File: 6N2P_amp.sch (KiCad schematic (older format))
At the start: 39 parts, among them J1 6.3MMTRSSwitched, U1 ECC83, U2 ECC83

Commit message: snap
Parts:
- added C14: 470p, Capacitor_THT:C_Rect_L9.0mm_W4.0mm_P7.50mm_MKT, symbol Device:C
- added C15: 22n, Capacitor_THT:C_Rect_L9.0mm_W4.0mm_P7.50mm_MKT, symbol Device:C
- added C16: 10n, Capacitor_THT:C_Rect_L9.0mm_W4.0mm_P7.50mm_MKT, symbol Device:C
- added R18, R19, R21, R22, R? (x2): LDR03, OptoDevice:R_LDR_10x8.5mm_P7.6mm_Vertical, symbol Sensor_Optical:LDR03
- added R20: 56k, Resistor_THT:R_Axial_DIN0207_L6.3mm_D2.5mm_P10.16mm_Horizontal, symbol Device:R
- added RV10: 50k lin, symbol Device:R_POT
- added RV11: 1M log, symbol Device:R_POT
- added RV7, RV9: 500k log, symbol Device:R_POT
- added RV8: 250k lin, symbol Device:R_POT
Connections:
- net GND: now also RV10.3, RV11.3, RV7.3
- net at C5.2, R7.2, U1.1 (A): now also R?.2
- net at C2.1, RV1.1: now also RV7.1
- net at C3.2, R4.2: now also R18.1, R19.1; no longer RV1.2
- net at R15.2, U2.6 (A): now also R?.2; no longer U2.2 (G)
- net at C11.2, R16.1, R17.1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: now also C14.2, R20.1
- net at RV6.2: now also R21.2
- new net: R18.2, RV1.2
- new net: R?.1, R?.1, U2.2 (G)
- new net: R19.2, RV7.2
- new net: RV10.1, RV9.3
- new net: C16.1, RV10.2
- new net: C15.1, RV8.3, RV9.1, RV9.2
- new net: C15.2, C16.2, R20.2
- new net: C14.1, RV8.1
- new net: RV11.1, RV8.2
- new net: R22.2, RV11.2
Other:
- note added: "clean channel"
- note added: "overdrive channel"
- moved on the sheet: C10, C11, C12, C13, C2, C3, C5, R14, R15, R17, R4, R5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

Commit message: it is making progress
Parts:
- added J2: 6.3MMTRSSwitched, micha_custom:Reichelt_EBS63P, symbol micha_custom:6.3MMTRSSwitched
- added R25, R29: 0R, Resistor_THT:R_Axial_DIN0207_L6.3mm_D2.5mm_P10.16mm_Horizontal, symbol Device:R
- added R26, R30: DNP, Resistor_THT:R_Axial_DIN0207_L6.3mm_D2.5mm_P10.16mm_Horizontal, symbol Device:R
- added R27: 5.6k, Resistor_THT:R_Axial_DIN0207_L6.3mm_D2.5mm_P10.16mm_Horizontal, symbol Device:R
- added R28, R31: 470R/1W, Resistor_THT:R_Axial_DIN0207_L6.3mm_D2.5mm_P10.16mm_Horizontal, symbol Device:R
- added TR1: TRANSF1, symbol Transformer:TRANSF1
- added U3: 6N1P, Valve:Valve_Noval_P, symbol micha_custom:6N1P
- gave numbers to parts that had none: 2
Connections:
- net GND: now also U1.9 (F2), U2.9 (F2), R26.1, R28.1, R30.1, U3.4 (F1), U3.9 (F2)
- net HV_C: now reaches C6.1, R10.2, R3.1, R7.1
- net at U1.4 (F1): now also R25.2, R26.2
- net 6.3V: now reaches U1.5 (F1)
- net 6.3V: now also U2.5 (F1), R25.1, R29.1, U3.5 (F1)
- net HV_B: now reaches C7.1, R10.1, R11.2, R15.1, U2.1 (A)
- net at U2.4 (F1): now also R29.2, R30.2
- net HV_A: now reaches C8.1, R11.1, R12.2
- net HV_A: now also TR1.2
- net HV_in: now reaches C9.1, R12.1, R13.2
- net at R22.1: now also R21.1, R27.2
- new net: TR1.1, U3.1 (A), U3.6 (A)
- new net: R27.1, U3.2 (G), U3.7 (G)
- new net: R28.2, U3.3 (K), U3.8 (K)
- new net: J2.3 (Sleeve), R31.2, TR1.3
- new net: J2.1 (Tip), TR1.4
- new net: J2.4 (TipSwitch), R31.1
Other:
- note added: "1W Power Amplifier"
- note added: "if U1 is 6N2P then\nR26=0R, R25=DNP"
- note removed: "6.3 between 4,5 for 6N2P"
- moved on the sheet: U2C

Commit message: some progress ... made symbols for dc dc converters and transformer
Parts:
- removed TR1: TRANSF1, symbol Transformer:TRANSF1
- added J? (x2): 6.3MMTRSSwitched, micha_custom:Reichelt_EBS63P, symbol micha_custom:6.3MMTRSSwitched
- added U? (x3): DSN-MINI-360, micha_custom:DSN-MINI-360, symbol micha_custom:DSN-MINI-360
- added U?: NCH6100HV, micha_custom:NCH6100HV, symbol micha_custom:NCH6100HV
- R31: value 470R/1W -> 8R/1W
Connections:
- net GND: now also J?.3 (Sleeve), J?.3 (Sleeve), U?.1 (GND), U?.2 (OUT-), U?.2 (OUT-), U?.2 (OUT-), U?.3 (IN-), U?.3 (IN-), U?.3 (IN-), U?.4 (GND)
- net HV_in: now also U?.5 (HV)
- net at R21.1, R22.1: now also J?.1 (Tip), J?.4 (TipSwitch); no longer R27.2
- removed net 6.3V: R25.1, R29.1, U1.5 (F1), U2.5 (F1), U3.5 (F1)
- new net: J?.1 (Tip), R27.2
- new net 12V: U?.3 (VIN), U?.4 (IN+), U?.4 (IN+), U?.4 (IN+)
- new net 6.3V_U1: R25.1, U1.5 (F1), U?.1 (OUT+)
- new net 6.3V_U2: R29.1, U2.5 (F1), U?.1 (OUT+)
- new net 6.3V_U3: U3.5 (F1), U?.1 (OUT+)
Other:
- note added: "FX return"
- note added: "FX send"
- note added: "adjust output\nto 6.3V !!!"
- moved on the sheet: C1, C10, C11, C12, C13, C14, C15, C16, C2, C3, C4, C5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

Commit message: snap, ... started experimental routing
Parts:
- removed U? (x3): DSN-MINI-360, micha_custom:DSN-MINI-360, symbol micha_custom:DSN-MINI-360
- added R32: DNP, Resistor_THT:R_Axial_DIN0204_L3.6mm_D1.6mm_P2.54mm_Vertical, symbol Device:R
- added R33: 0R, Resistor_THT:R_Axial_DIN0204_L3.6mm_D1.6mm_P2.54mm_Vertical, symbol Device:R
- added TR1: VISATON_TR_10.16, micha_custom:VISATON_TR_10.16, symbol micha_custom:VISATON_TR_10.16
- added U4, U5, U6: DSN-MINI-360, micha_custom:DSN-MINI-360, symbol micha_custom:DSN-MINI-360
- J2: value 6.3MMTRSSwitched -> speaker
- J3: renamed from J?; value 6.3MMTRSSwitched -> fx_send
- J4: renamed from J?; value 6.3MMTRSSwitched -> fx_return
- R25, R26, R29, R30: footprint Resistor_THT:R_Axial_DIN0207_L6.3mm_D2.5mm_P10.16mm_Horizontal -> Resistor_THT:R_Axial_DIN0204_L3.6mm_D1.6mm_P2.54mm_Vertical
- RV1, RV10, RV11, RV2, RV3, RV4, RV5, RV6, RV7, RV8, RV9: footprint (none) -> Potentiometer_THT:Potentiometer_Alps_RK163_Single_Horizontal
- U3: footprint Valve:Valve_Noval_P -> w_vacuum:socket_gzc9-b
- gave numbers to parts that had none: 1
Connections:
- net 12V: now also U4.4 (IN+), U5.4 (IN+), U6.4 (IN+)
- net 6.3V_U1: now also U4.1 (OUT+)
- net 6.3V_U2: now also U5.1 (OUT+)
- net 6.3V_U3: now also R32.1, U6.1 (OUT+)
- net GND: now also RV1.1, RV10.1, RV11.1, RV2.1, RV5.1, RV6.1, RV7.1, R33.1, U4.2 (OUT-), U4.3 (IN-), U5.2 (OUT-), U5.3 (IN-), U6.2 (OUT-), U6.3 (IN-); no longer RV1.3, RV10.3, RV11.3, RV2.3, RV5.3, RV6.3, RV7.3, U3.4 (F1)
- net HV_A: now also TR1.2
- net at C5.1: now also RV2.3; no longer RV2.1
- net at RV4.3: now also C12.1, RV3.1, RV4.2; no longer RV5.1
- net at C11.1: now also RV3.3; no longer RV3.1
- net at RV3.2: now also RV6.3; no longer RV6.1
- net at RV9.3: now also C15.1, RV8.1, RV9.2; no longer RV10.1
- net at C14.1: now also RV8.3; no longer RV8.1
- net at RV8.2: now also RV11.3; no longer RV11.1
- net at U3.1 (A), U3.6 (A): now also TR1.1
- net at J2.1 (Tip): now also TR1.4
- net at J2.3 (Sleeve), R31.2: now also TR1.3
- new net: C2.1, RV1.3, RV7.3
- new net: RV4.1, RV5.3
- new net: RV10.3, RV9.1
- new net: R32.2, R33.2, U3.4 (F1)
- no-connect marks 3 -> 14
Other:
- moved on the sheet: U3C

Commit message: snap
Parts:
- J1: value 6.3MMTRSSwitched -> guitar_in
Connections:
- net guit_in: now reaches J1.1 (Tip), R1.1, U1.7 (G)
- net clean_channel_bypass: now reaches C5.2, R24.2, R7.2, U1.1 (A)
- net post_stage_1: now reaches C2.1, RV1.3, RV7.3
- net od_A: now reaches R15.2, R23.2, U2.6 (A)
- net fx_send: now reaches J3.1 (Tip), J4.4 (TipSwitch), R21.1, R22.1
- net power_anode: now reaches TR1.1, U3.1 (A), U3.6 (A)
- net spkr_n: now reaches J2.3 (Sleeve), R31.2, TR1.3
- net spkr_p: now reaches J2.1 (Tip), TR1.4
- net power_gate: now reaches R27.1, U3.2 (G), U3.7 (G)
- net power_cath: now reaches R28.2, U3.3 (K), U3.8 (K)
- net fx_return: now reaches J4.1 (Tip), R27.2
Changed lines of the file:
@@
 P 4100 8550
 F 0 "J1" H 4063 8697 60  0000 C CNN
-F 1 "6.3MMTRSSwitched" H 4063 8591 60  0000 C CNN
+F 1 "guitar_in" H 4063 8591 60  0000 C CNN
 F 2 "micha_custom:Reichelt_EBS63P" H 4100 8550 60  0001 C CNN
 F 3 "" H 4100 8550 60  0000 C CNN
@@
 NoConn ~ 2000 5600
 NoConn ~ 11250 3950
+Text Label 13600 3000 0    50   ~ 0
+fx_send
+Text Label 14050 3400 0    50   ~ 0
+fx_return
+Text Label 15100 4550 0    50   ~ 0
+power_anode
+Text Label 14900 5550 0    50   ~ 0
+power_gate
+Text Label 15000 5650 0    50   ~ 0
+power_cath
+Text Label 17300 4550 0    50   ~ 0
+spkr_p
+Text Label 17300 4750 0    50   ~ 0
+spkr_n
+Text Label 4900 8650 0    50   ~ 0
+guit_in
+Text Label 7150 8150 0    50   ~ 0
+post_stage_1
+Text Label 10850 12000 0    50   ~ 0
+clean_channel_bypass
+Text Label 12700 8150 0    50   ~ 0
+od_A
 $EndSCHEMATC

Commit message: snap
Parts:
- R25, R29: value 0R -> ECC83
- R26, R30: value DNP -> 6N2P
- R32: value DNP -> ECCXX
- R33: value 0R -> 6N1P
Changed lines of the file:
@@
 P 2000 2500
 F 0 "R25" V 1793 2500 50  0000 C CNN
-F 1 "0R" V 1884 2500 50  0000 C CNN
+F 1 "ECC83" V 1884 2500 50  0000 C CNN
 F 2 "Resistor_THT:R_Axial_DIN0204_L3.6mm_D1.6mm_P2.54mm_Vertical" V 1930 2500 50  0001 C CNN
 F 3 "~" H 2000 2500 50  0001 C CNN
@@
 P 2000 2650
 F 0 "R26" V 2150 2650 50  0000 C CNN
-F 1 "DNP" V 2250 2650 50  0000 C CNN
+F 1 "6N2P" V 2250 2650 50  0000 C CNN
 F 2 "Resistor_THT:R_Axial_DIN0204_L3.6mm_D1.6mm_P2.54mm_Vertical" V 1930 2650 50  0001 C CNN
 F 3 "~" H 2000 2650 50  0001 C CNN
@@
 P 2000 4000
 F 0 "R29" V 1793 4000 50  0000 C CNN
-F 1 "0R" V 1884 4000 50  0000 C CNN
+F 1 "ECC83" V 1884 4000 50  0000 C CNN
 F 2 "Resistor_THT:R_Axial_DIN0204_L3.6mm_D1.6mm_P2.54mm_Vertical" V 1930 4000 50  0001 C CNN
 F 3 "~" H 2000 4000 50  0001 C CNN
@@
 P 2000 4150
 F 0 "R30" V 2150 4150 50  0000 C CNN
-F 1 "DNP" V 2250 4150 50  0000 C CNN
+F 1 "6N2P" V 2250 4150 50  0000 C CNN
 F 2 "Resistor_THT:R_Axial_DIN0204_L3.6mm_D1.6mm_P2.54mm_Vertical" V 1930 4150 50  0001 C CNN
 F 3 "~" H 2000 4150 50  0001 C CNN
@@
 P 2000 5750
 F 0 "R33" V 2200 5750 50  0000 C CNN
-F 1 "0R" V 2100 5750 50  0000 C CNN
+F 1 "6N1P" V 2100 5750 50  0000 C CNN
 F 2 "Resistor_THT:R_Axial_DIN0204_L3.6mm_D1.6mm_P2.54mm_Vertical" V 1930 5750 50  0001 C CNN
 F 3 "~" H 2000 5750 50  0001 C CNN
@@
 P 2000 5600
 F 0 "R32" V 1900 5600 50  0000 C CNN
-F 1 "DNP" V 1800 5600 50  0000 C CNN
+F 1 "ECCXX" V 1800 5600 50  0000 C CNN
 F 2 "Resistor_THT:R_Axial_DIN0204_L3.6mm_D1.6mm_P2.54mm_Vertical" V 1930 5600 50  0001 C CNN
 F 3 "~" H 2000 5600 50  0001 C CNN

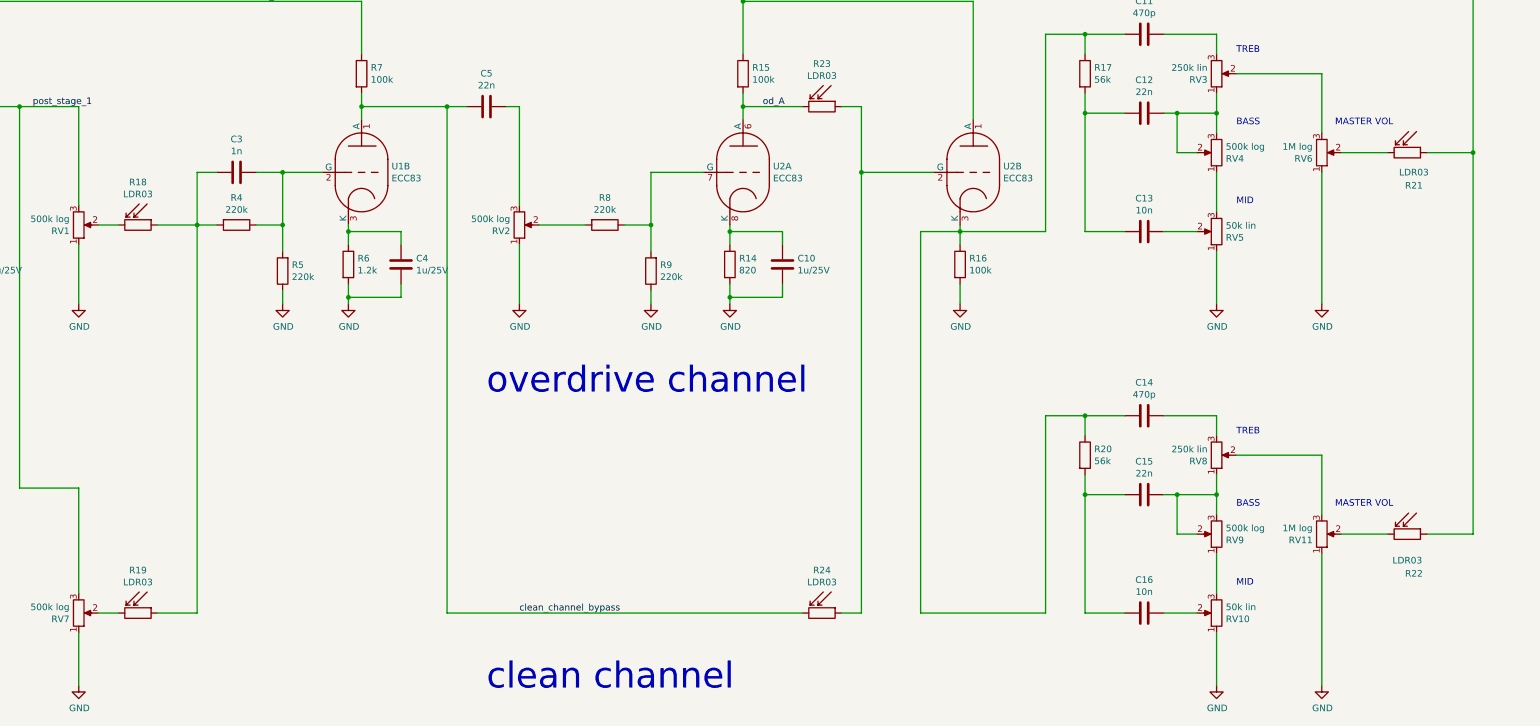
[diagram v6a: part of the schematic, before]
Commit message: added the ldr leds
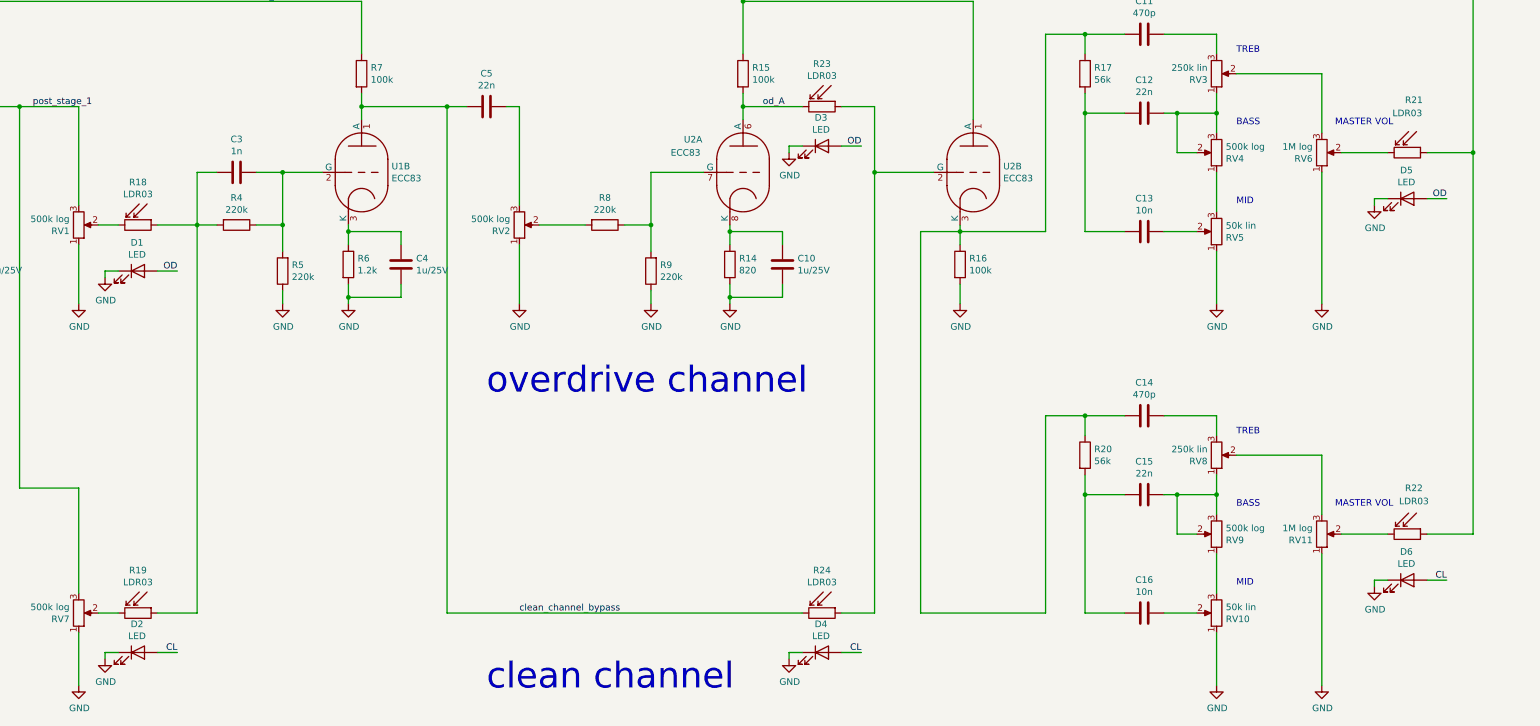
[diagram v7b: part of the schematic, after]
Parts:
- added D1, D2, D3, D4, D5, D6: LED, LED_THT:LED_D5.0mm, symbol Device:LED
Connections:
- net GND: now also D1.1 (K), D2.1 (K), D3.1 (K), D4.1 (K), D5.1 (K), D6.1 (K)
- new net CL: D2.2 (A), D4.2 (A), D6.2 (A)
- new net OD: D1.2 (A), D3.2 (A), D5.2 (A)
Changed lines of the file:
@@
 U 1 1 5EA1B1F1
 P 12550 8650
-F 0 "U2" H 12778 8696 50  0000 L CNN
-F 1 "ECC83" H 12778 8605 50  0000 L CNN
+F 0 "U2" H 12100 8900 50  0000 L CNN
+F 1 "ECC83" H 12000 8800 50  0000 L CNN
 F 2 "w_vacuum:tube_gzc9-b" H 12820 8250 50  0001 C CNN
 F 3 "http://www.r-type.org/pdfs/ecc83.pdf" H 12550 8650 50  0001 C CNN
@@
 U 1 1 5EDAA599
 P 17600 11400
-F 0 "R22" V 17900 11450 50  0000 C CNN
-F 1 "LDR03" V 17800 11400 50  0000 C CNN
+F 0 "R22" V 17250 11450 50  0000 C CNN
+F 1 "LDR03" V 17350 11450 50  0000 C CNN
 F 2 "OptoDevice:R_LDR_10x8.5mm_P7.6mm_Vertical" V 17775 11400 50  0001 C CNN
 F 3 "http://www.elektronica-componenten.nl/WebRoot/StoreNL/Shops/61422969/54F1/BA0C/C664/31B9/2173/C0A8/2AB9/2AEF/LDR03IMP.pdf" H 17600 11350 50  0001 C CNN
@@
 U 1 1 5EDAA59F
 P 17600 8500
-F 0 "R21" V 17850 8550 50  0000 C CNN
-F 1 "LDR03" V 17750 8550 50  0000 C CNN
+F 0 "R21" V 17200 8550 50  0000 C CNN
+F 1 "LDR03" V 17300 8500 50  0000 C CNN
 F 2 "OptoDevice:R_LDR_10x8.5mm_P7.6mm_Vertical" V 17775 8500 50  0001 C CNN
 F 3 "http://www.elektronica-componenten.nl/WebRoot/StoreNL/Shops/61422969/54F1/BA0C/C664/31B9/2173/C0A8/2AB9/2AEF/LDR03IMP.pdf" H 17600 8450 50  0001 C CNN
@@
 Wire Wire Line
 	10300 8150 10450 8150
-Connection ~ 13450 8650
-Wire Wire Line
-	13450 8650 14000 8650
-Wire Wire Line
-	13450 8150 13450 8650
 $Comp
 L Sensor_Optical:LDR03 R23
@@
 	0    1    1    0
 $EndComp
-Wire Wire Line
-	13300 8150 13450 8150
 $Comp
 L Sensor_Optical:LDR03 R24
@@
 	0    1    1    0
 $EndComp
-Wire Wire Line
-	13300 12000 13450 12000
-Wire Wire Line
-	13450 8650 13450 12000
 Wire Wire Line
 	10300 8150 10300 12000
@@
 Text Label 12700 8150 0    50   ~ 0
 od_A
+$Comp
+L Device:LED D1
+U 1 1 5F57B25A
+P 7950 9400
+F 0 "D1" H 7943 9616 50  0000 C CNN
+F 1 "LED" H 7943 9525 50  0000 C CNN
+F 2 "LED_THT:LED_D5.0mm" H 7950 9400 50  0001 C CNN
+F 3 "~" H 7950 9400 50  0001 C CNN
+	1    7950 9400
+	1    0    0    -1
+$EndComp
+$Comp
+L power:GND #PWR033
+U 1 1 5F57EB92
+P 7700 9450
+F 0 "#PWR033" H 7700 9200 50  0001 C CNN
+F 1 "GND" H 7705 9277 50  0000 C CNN
+F 2 "" H 7700 9450 50  0001 C CNN
+F 3 "" H 7700 9450 50  0001 C CNN
+	1    7700 9450
+	1    0    0    -1
+$EndComp
+Wire Wire Line
+	7800 9400 7700 9400
+Wire Wire Line
+	7700 9400 7700 9450
+Wire Wire Line
+	8100 9400 8250 9400
+Text Label 8250 9400 2    50   ~ 0
+OD
+$Comp
+L Device:LED D2
+U 1 1 5F5B6232
+P 7950 12300
+F 0 "D2" H 7943 12516 50  0000 C CNN
+F 1 "LED" H 7943 12425 50  0000 C CNN
+F 2 "LED_THT:LED_D5.0mm" H 7950 12300 50  0001 C CNN
+F 3 "~" H 7950 12300 50  0001 C CNN
+	1    7950 12300
+	1    0    0    -1
+$EndComp
+$Comp
+L power:GND #PWR034
+U 1 1 5F5B623C
+P 7700 12350
+F 0 "#PWR034" H 7700 12100 50  0001 C CNN
+F 1 "GND" H 7705 12177 50  0000 C CNN
+F 2 "" H 7700 12350 50  0001 C CNN
+F 3 "" H 7700 12350 50  0001 C CNN
+	1    7700 12350
+	1    0    0    -1
+$EndComp
+Wire Wire Line
+	7800 12300 7700 12300
+Wire Wire Line
+	7700 12300 7700 12350
+Wire Wire Line
+	8100 12300 8250 12300
+Text Label 8250 12300 2    50   ~ 0
+CL
+$Comp
+L Device:LED D4
+U 1 1 5F5F4659
+P 13150 12300
+F 0 "D4" H 13143 12516 50  0000 C CNN
+F 1 "LED" H 13143 12425 50  0000 C CNN
+F 2 "LED_THT:LED_D5.0mm" H 13150 12300 50  0001 C CNN
+F 3 "~" H 13150 12300 50  0001 C CNN
+	1    13150 12300
+	1    0    0    -1
+$EndComp
+$Comp
+L power:GND #PWR036
+U 1 1 5F5F4663
+P 12900 12350
+F 0 "#PWR036" H 12900 12100 50  0001 C CNN
+F 1 "GND" H 12905 12177 50  0000 C CNN
+F 2 "" H 12900 12350 50  0001 C CNN
+F 3 "" H 12900 12350 50  0001 C CNN
+	1    12900 12350
+	1    0    0    -1
+$EndComp
+Wire Wire Line
+	13000 12300 12900 12300
+Wire Wire Line
+	12900 12300 12900 12350
+Wire Wire Line
+	13300 12300 13450 12300
+Text Label 13450 12300 2    50   ~ 0
+CL
+$Comp
+L Device:LED D6
+U 1 1 5F6201D0
+P 17600 11750
+F 0 "D6" H 17593 11966 50  0000 C CNN
+F 1 "LED" H 17593 11875 50  0000 C CNN
+F 2 "LED_THT:LED_D5.0mm" H 17600 11750 50  0001 C CNN
+F 3 "~" H 17600 11750 50  0001 C CNN
+	1    17600 11750
+	1    0    0    -1
+$EndComp
+$Comp
+L power:GND #PWR038
+U 1 1 5F6201DA
+P 17350 11800
+F 0 "#PWR038" H 17350 11550 50  0001 C CNN
+F 1 "GND" H 17355 11627 50  0000 C CNN
+F 2 "" H 17350 11800 50  0001 C CNN
+F 3 "" H 17350 11800 50  0001 C CNN
+	1    17350 11800
+	1    0    0    -1
+$EndComp
+Wire Wire Line
+	17450 11750 17350 11750
+Wire Wire Line
+	17350 11750 17350 11800
+Wire Wire Line
+	17750 11750 17900 11750
+Text Label 17900 11750 2    50   ~ 0
+CL
+$Comp
+L Device:LED D5
+U 1 1 5F69233B
+P 17600 8850
+F 0 "D5" H 17593 9066 50  0000 C CNN
+F 1 "LED" H 17593 8975 50  0000 C CNN
+F 2 "LED_THT:LED_D5.0mm" H 17600 8850 50  0001 C CNN
+F 3 "~" H 17600 8850 50  0001 C CNN
+	1    17600 8850
+	1    0    0    -1
+$EndComp
+$Comp
+L power:GND #PWR037
+U 1 1 5F692345
+P 17350 8900
+F 0 "#PWR037" H 17350 8650 50  0001 C CNN
+F 1 "GND" H 17355 8727 50  0000 C CNN
+F 2 "" H 17350 8900 50  0001 C CNN
+F 3 "" H 17350 8900 50  0001 C CNN
+	1    17350 8900
+	1    0    0    -1
+$EndComp
+Wire Wire Line
+	17450 8850 17350 8850
+Wire Wire Line
+	17750 8850 17900 8850
+Text Label 17900 8850 2    50   ~ 0
+OD
+Wire Wire Line
+	17350 8900 17350 8850
+Connection ~ 13550 8650
+Wire Wire Line
+	13550 8650 14000 8650
+Wire Wire Line
+	13550 8150 13550 8650
+Wire Wire Line
+	13300 8150 13550 8150
+Wire Wire Line
+	13300 12000 13550 12000
+Wire Wire Line
+	13550 8650 13550 12000
+$Comp
+L Device:LED D3
+U 1 1 5F7530BE
+P 13150 8450
+F 0 "D3" H 13143 8666 50  0000 C CNN
+F 1 "LED" H 13143 8575 50  0000 C CNN
+F 2 "LED_THT:LED_D5.0mm" H 13150 8450 50  0001 C CNN
+F 3 "~" H 13150 8450 50  0001 C CNN
+	1    13150 8450
+	1    0    0    -1
+$EndComp
+$Comp
+L power:GND #PWR035
+U 1 1 5F7530C8
+P 12900 8500
+F 0 "#PWR035" H 12900 8250 50  0001 C CNN
+F 1 "GND" H 12905 8327 50  0000 C CNN
+F 2 "" H 12900 8500 50  0001 C CNN
+F 3 "" H 12900 8500 50  0001 C CNN
+	1    12900 8500
+	1    0    0    -1
+$EndComp
+Wire Wire Line
+	13000 8450 12900 8450
+Wire Wire Line
+	13300 8450 13450 8450
+Text Label 13450 8450 2    50   ~ 0
+OD
+Wire Wire Line
+	12900 8500 12900 8450
 $EndSCHEMATC

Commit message: snap
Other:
- note added: "TODO:\nLDR footprints are too big\nfootswitch -> 2n7000 inverter to swith CL and OD nets"
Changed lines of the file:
@@
 Wire Wire Line
 	12900 8500 12900 8450
+Text Notes 1550 13600 0    118  ~ 0
+TODO:\nLDR footprints are too big\nfootswitch -> 2n7000 inverter to swith CL and OD nets
 $EndSCHEMATC
